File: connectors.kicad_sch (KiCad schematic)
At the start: 48 parts, among them J18 PinHeader_1x4_P2.5mm_Drill1mm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, J19 PinHeader_1x2_P2.5mm_Drill1mm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, J6 10107844-002LF, J7 JST_XH_1x2_S2B-XH-A-LF-SN, Q8 BC807-25W, SW1 MSS3-V-T_R, U10 USB-C_GCT_USB4145-03-0070-C

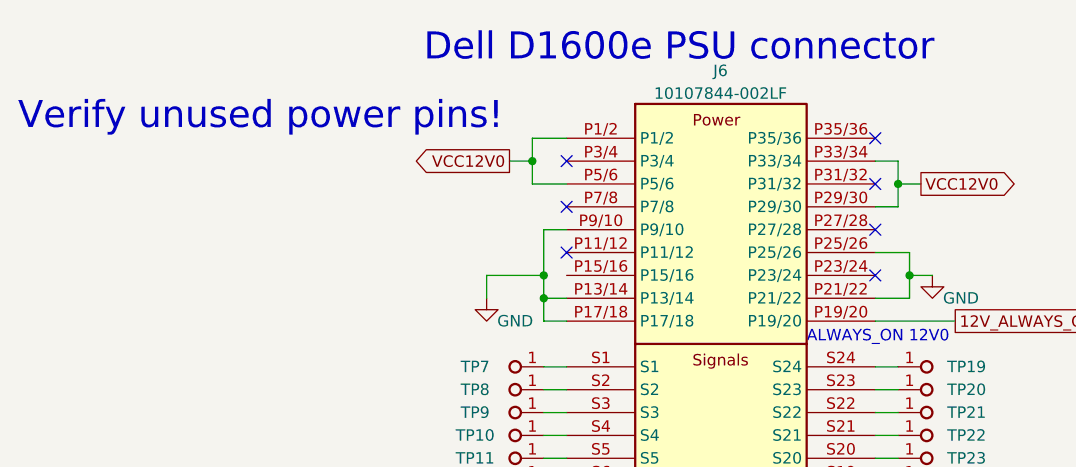
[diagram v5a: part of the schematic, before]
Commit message: Updated d1600e connections
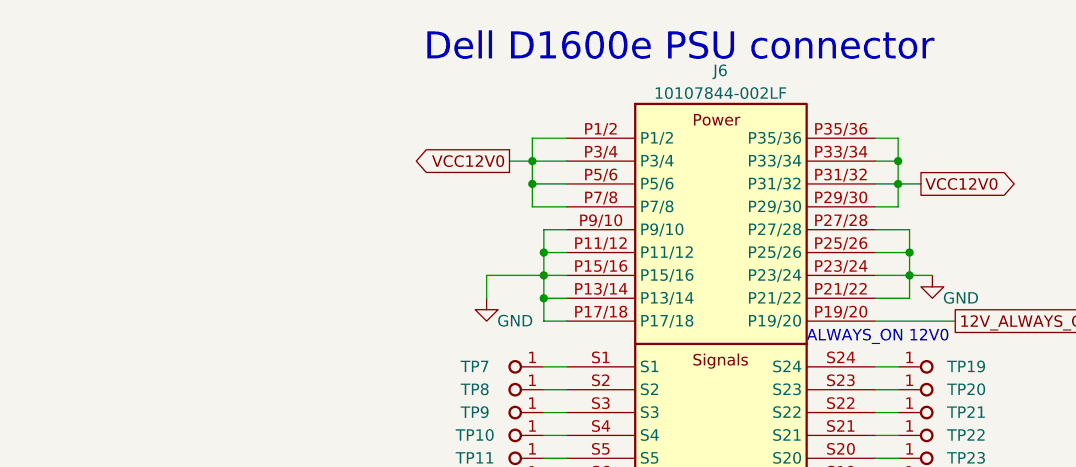
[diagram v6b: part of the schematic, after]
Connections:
- net GND: now also J6.P11/12, J6.P15/16, J6.P23/24, J6.P27/28
- net VCC12V0: now also J6.P3/4, J6.P31/32, J6.P35/36, J6.P7/8
- no-connect marks 8 -> 1
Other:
- note removed: "Verify unused power pins!"
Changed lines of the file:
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@@
   (junction (at 119.38 107.95) (diameter 0) (color 0 0 0 0)
   )
+  (junction (at 80.01 115.57) (diameter 0) (color 0 0 0 0)
+  )
   (junction (at 120.65 118.11) (diameter 0) (color 0 0 0 0)
   )
@@
   (junction (at 190.5 132.08) (diameter 0) (color 0 0 0 0)
   )
+  (junction (at 119.38 105.41) (diameter 0) (color 0 0 0 0)
+  )
   (junction (at 78.74 105.41) (diameter 0) (color 0 0 0 0)
   )
@@
   (junction (at 190.5 143.51) (diameter 0) (color 0 0 0 0)
   )
+  (junction (at 120.65 115.57) (diameter 0) (color 0 0 0 0)
+  )
+  (junction (at 78.74 107.95) (diameter 0) (color 0 0 0 0)
+  )
   (junction (at 118.11 153.67) (diameter 0) (color 0 0 0 0)
   )
@@
   )
   (no_connect (at 205.74 129.54))
-  (no_connect (at 116.84 118.11))
-  (no_connect (at 82.55 115.57))
-  (no_connect (at 82.55 105.41))
-  (no_connect (at 116.84 107.95))
-  (no_connect (at 116.84 113.03))
-  (no_connect (at 82.55 110.49))
-  (no_connect (at 116.84 102.87))
   (wire (pts (xy 78.74 102.87) (xy 78.74 105.41))
     (stroke (width 0) (type default) (color 0 0 0 0))
@@
     (stroke (width 0) (type default) (color 0 0 0 0))
   )
+  (wire (pts (xy 78.74 105.41) (xy 82.55 105.41))
+    (stroke (width 0) (type default) (color 0 0 0 0))
+  )
   (wire (pts (xy 290.83 139.7) (xy 303.53 139.7))
     (stroke (width 0) (type default) (color 0 0 0 0))
@@
     (stroke (width 0) (type default) (color 0 0 0 0))
   )
+  (wire (pts (xy 80.01 115.57) (xy 82.55 115.57))
+    (stroke (width 0) (type default) (color 0 0 0 0))
+  )
   (wire (pts (xy 119.38 105.41) (xy 119.38 107.95))
     (stroke (width 0) (type default) (color 0 0 0 0))
@@
     (stroke (width 0) (type default) (color 0 0 0 0))
   )
+  (wire (pts (xy 80.01 115.57) (xy 80.01 118.11))
+    (stroke (width 0) (type default) (color 0 0 0 0))
+  )
   (wire (pts (xy 353.06 106.68) (xy 360.68 106.68))
     (stroke (width 0) (type default) (color 0 0 0 0))
@@
     (stroke (width 0) (type default) (color 0 0 0 0))
   )
-  (wire (pts (xy 80.01 113.03) (xy 80.01 118.11))
+  (wire (pts (xy 80.01 118.11) (xy 82.55 118.11))
+    (stroke (width 0) (type default) (color 0 0 0 0))
+  )
+  (wire (pts (xy 119.38 102.87) (xy 119.38 105.41))
+    (stroke (width 0) (type default) (color 0 0 0 0))
+  )
+  (wire (pts (xy 80.01 113.03) (xy 80.01 115.57))
     (stroke (width 0) (type default) (color 0 0 0 0))
   )
@@
     (stroke (width 0) (type default) (color 0 0 0 0))
   )
+  (wire (pts (xy 120.65 113.03) (xy 120.65 115.57))
+    (stroke (width 0) (type default) (color 0 0 0 0))
+  )
   (wire (pts (xy 80.01 130.81) (xy 82.55 130.81))
     (stroke (width 0) (type default) (color 0 0 0 0))
@@
     (stroke (width 0) (type default) (color 0 0 0 0))
   )
+  (wire (pts (xy 82.55 110.49) (xy 78.74 110.49))
+    (stroke (width 0) (type default) (color 0 0 0 0))
+  )
   (wire (pts (xy 197.485 227.33) (xy 197.485 217.17))
     (stroke (width 0) (type default) (color 0 0 0 0))
@@
     (stroke (width 0) (type default) (color 0 0 0 0))
   )
+  (wire (pts (xy 116.84 102.87) (xy 119.38 102.87))
+    (stroke (width 0) (type default) (color 0 0 0 0))
+  )
   (wire (pts (xy 80.01 118.11) (xy 80.01 120.65))
     (stroke (width 0) (type default) (color 0 0 0 0))
@@
     (stroke (width 0) (type default) (color 0 0 0 0))
   )
+  (wire (pts (xy 116.84 107.95) (xy 119.38 107.95))
+    (stroke (width 0) (type default) (color 0 0 0 0))
+  )
   (wire (pts (xy 78.74 105.41) (xy 78.74 107.95))
     (stroke (width 0) (type default) (color 0 0 0 0))
@@
     (stroke (width 0) (type default) (color 0 0 0 0))
   )
+  (wire (pts (xy 116.84 118.11) (xy 120.65 118.11))
+    (stroke (width 0) (type default) (color 0 0 0 0))
+  )
   (wire (pts (xy 361.95 113.665) (xy 322.58 113.665))
     (stroke (width 0) (type default) (color 0 0 0 0))
@@
     (stroke (width 0) (type default) (color 0 0 0 0))
   )
+  (wire (pts (xy 116.84 113.03) (xy 120.65 113.03))
+    (stroke (width 0) (type default) (color 0 0 0 0))
+  )
   (wire (pts (xy 82.55 102.87) (xy 78.74 102.87))
     (stroke (width 0) (type default) (color 0 0 0 0))
@@
   )
   (wire (pts (xy 303.53 102.87) (xy 303.53 105.41))
+    (stroke (width 0) (type default) (color 0 0 0 0))
+  )
+  (wire (pts (xy 78.74 110.49) (xy 78.74 107.95))
     (stroke (width 0) (type default) (color 0 0 0 0))
   )
@@
     (effects (font (size 1.27 1.27)) (justify left bottom))
   )
-  (text "Verify unused power pins!" (at 21.59 102.235 0)
-    (effects (font (size 2.9972 2.9972)) (justify left bottom))
-  )
   (text "ALWAYS_ON 12V0\n" (at 109.22 125.73 0)

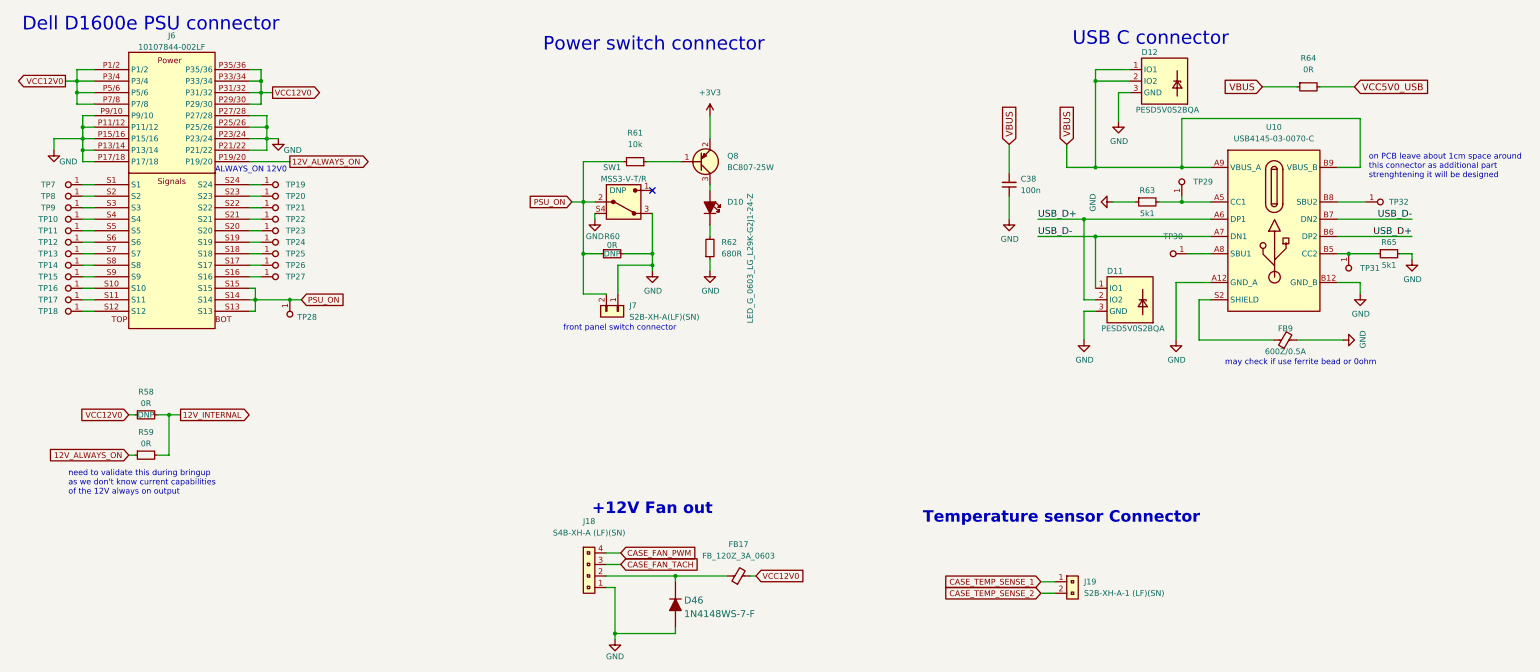
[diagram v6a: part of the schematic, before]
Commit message: Minor fixes in schematic layout and reannotate
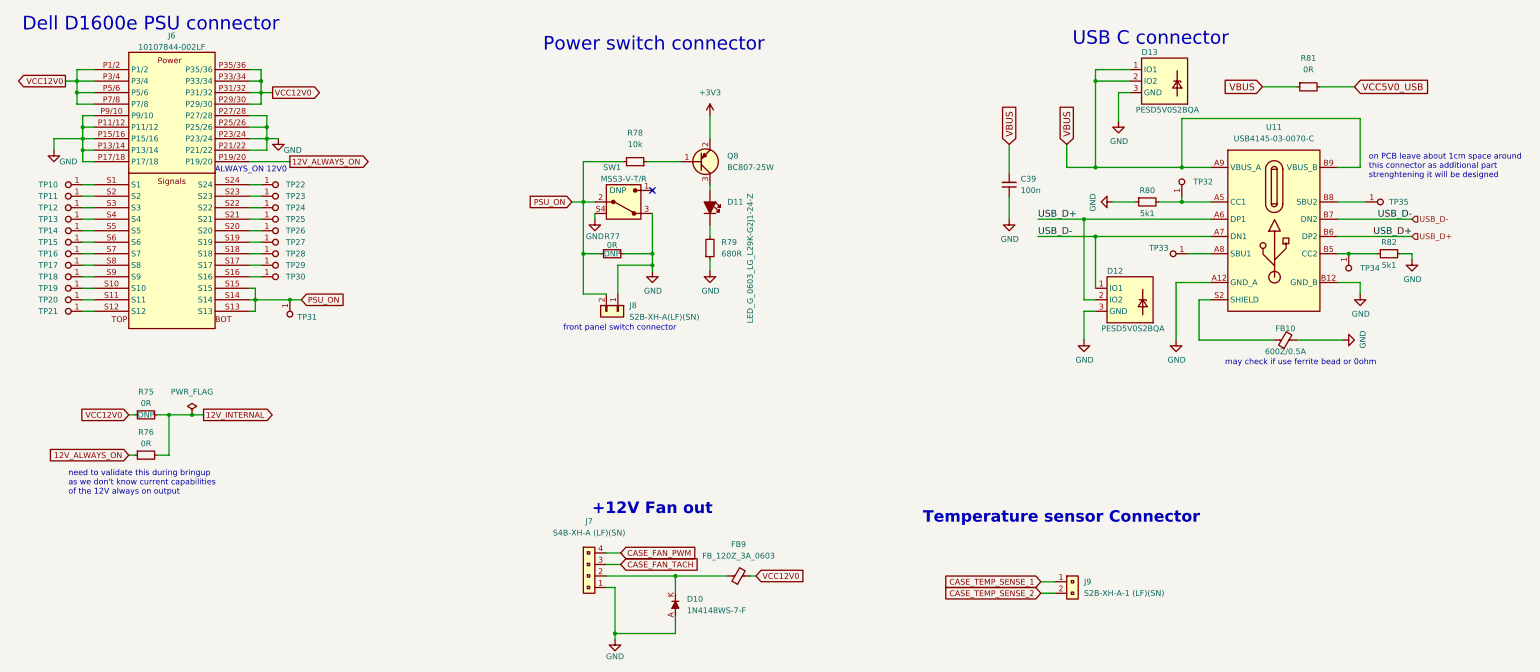
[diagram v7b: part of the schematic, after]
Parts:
- removed D46: 1N4148WS-7-F, antmicro-footprints:SOD-323, symbol antmicroDiodesRectifiersSingle:1N4148WS-7-F
- added D10: 1N4148WS-7-F, antmicro-footprints:SOD-323, symbol antmicroDiodesRectifiersSingle:1N4148WS-7-F
- renumbered C38 to C39, D10 to D11, D11 to D12, D12 to D13, FB9 to FB10, FB17 to FB9, J18 to J7, J7 to J8, J19 to J9, R58 to R75, R59 to R76, R60 to R77, R61 to R78, R62 to R79, R63 to R80, R64 to R81, R65 to R82, TP7 to TP10, TP8 to TP11, TP9 to TP12, TP10 to TP13, TP11 to TP14, TP12 to TP15, TP13 to TP16, TP14 to TP17, TP15 to TP18, TP16 to TP19, TP17 to TP20, TP18 to TP21, TP19 to TP22, TP20 to TP23, TP21 to TP24, TP22 to TP25, TP23 to TP26, TP24 to TP27, TP25 to TP28, TP26 to TP29, TP27 to TP30, TP28 to TP31, TP29 to TP32, TP30 to TP33, TP31 to TP34, TP32 to TP35, U10 to U11
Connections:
- net GND: now also D10.A
- net at FB9.1, J7.2: now also D10.K

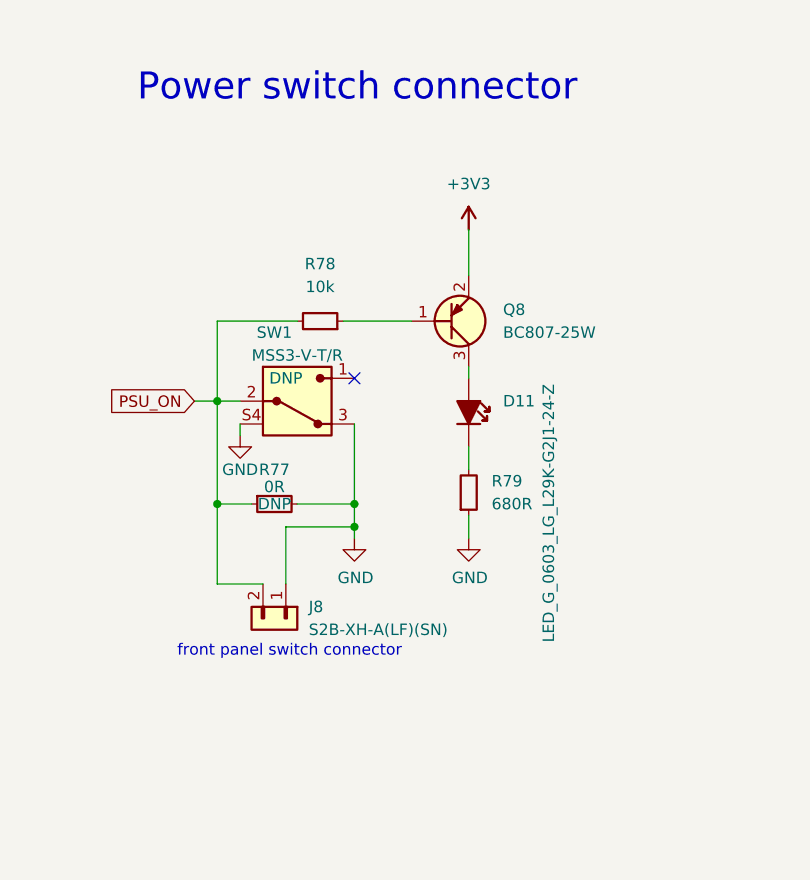
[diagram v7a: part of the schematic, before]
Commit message: Redesign power LED indicator
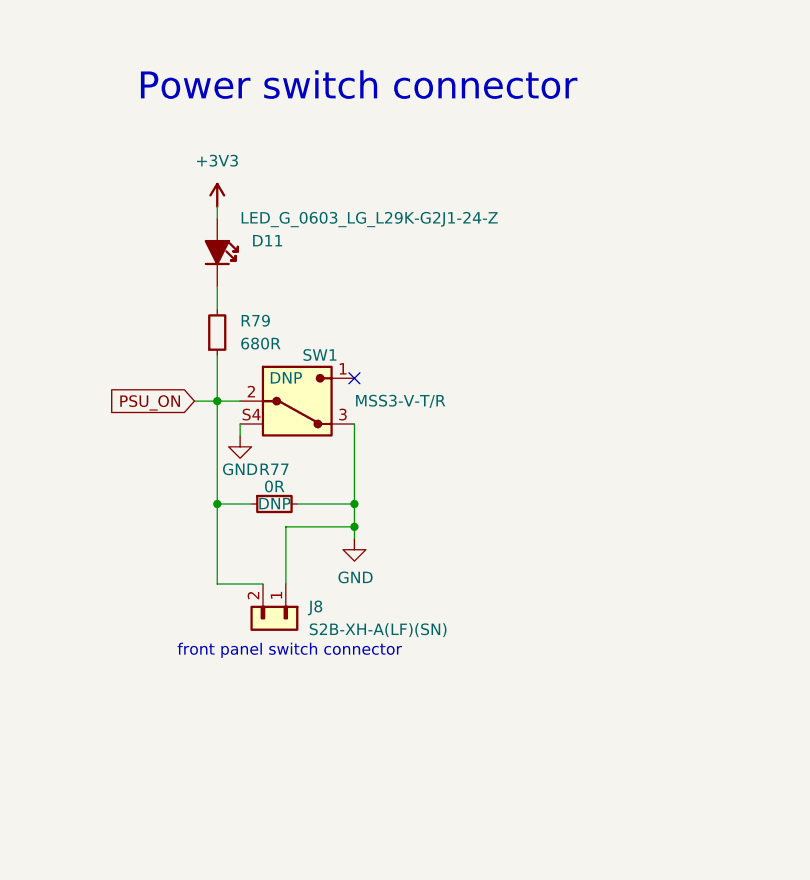
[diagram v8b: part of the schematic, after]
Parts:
- removed Q8: BC807-25W, antmicro-footprints:SOT-323, symbol antmicroTransistorsBipolarSingle:BC807-25W
- removed R78: R_10k_0402, antmicro-footprints:R_0402_1005Metric, symbol antmicroResistors0402:R_10k_0402
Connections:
- net +3V3: now also D11.1
- net GND: no longer R79.1
- net PSU_ON: now also R79.1
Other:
- moved on the sheet: D11, R79
